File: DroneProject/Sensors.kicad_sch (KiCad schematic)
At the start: 21 parts, among them U61 LSM6DSOTR, U62 TMAG5273C1QDBVR, U63 INA181A1IDBVR, U64 M24C02-WMN6TP

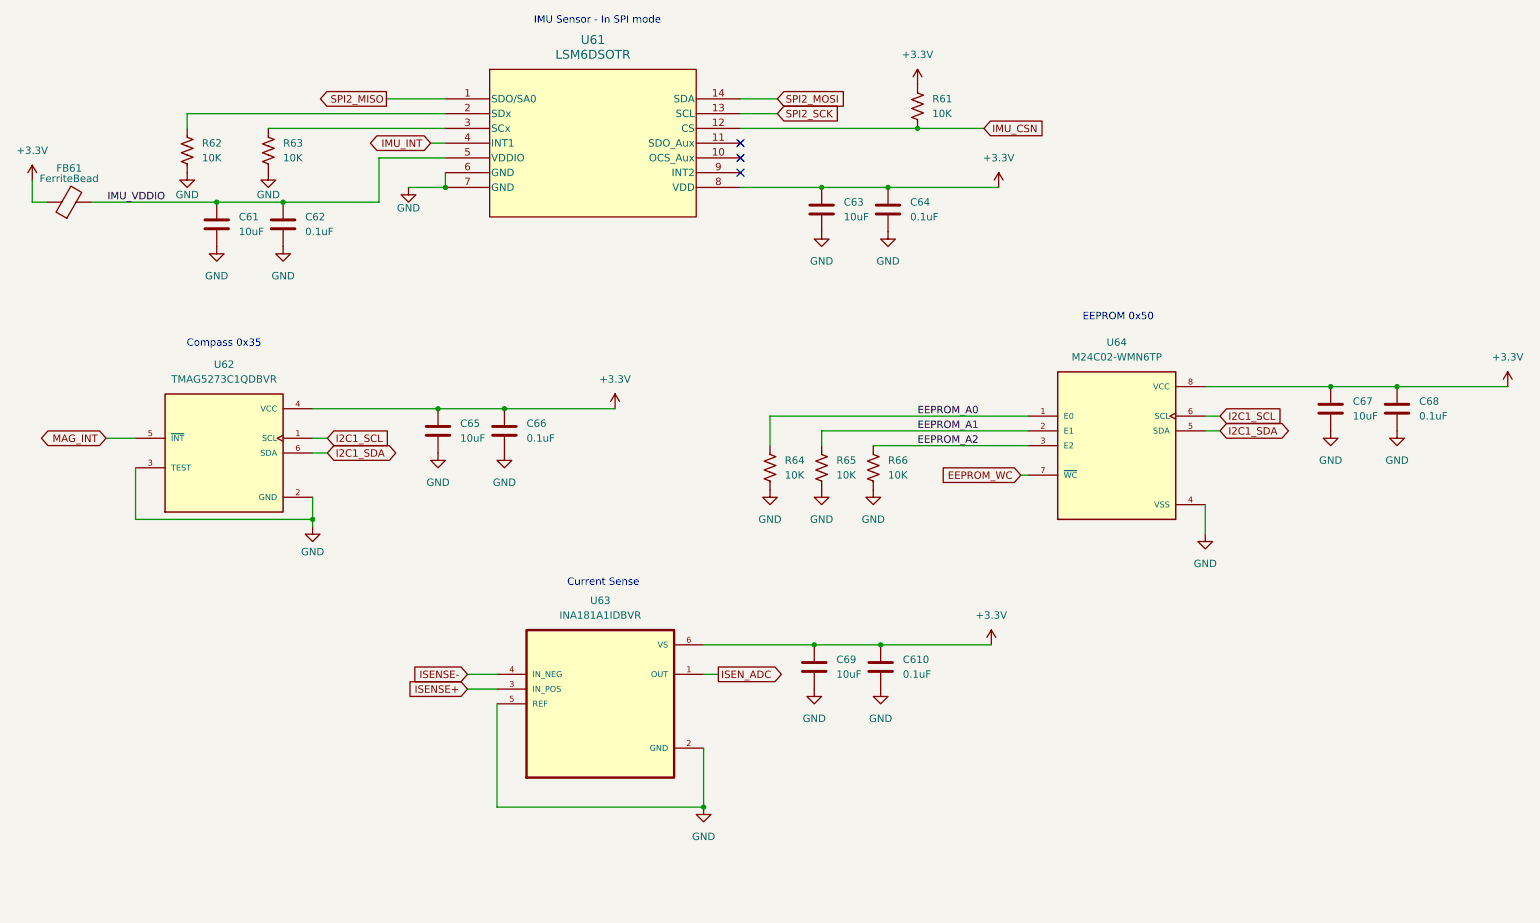
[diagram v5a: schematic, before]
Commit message: Changed motor controller to higher pin count MCU.  Defined all the pins for 3x PWM control over 4 motors.  Renamed a couple of global IO signals to indicate MCU origin (C0 vs C1)
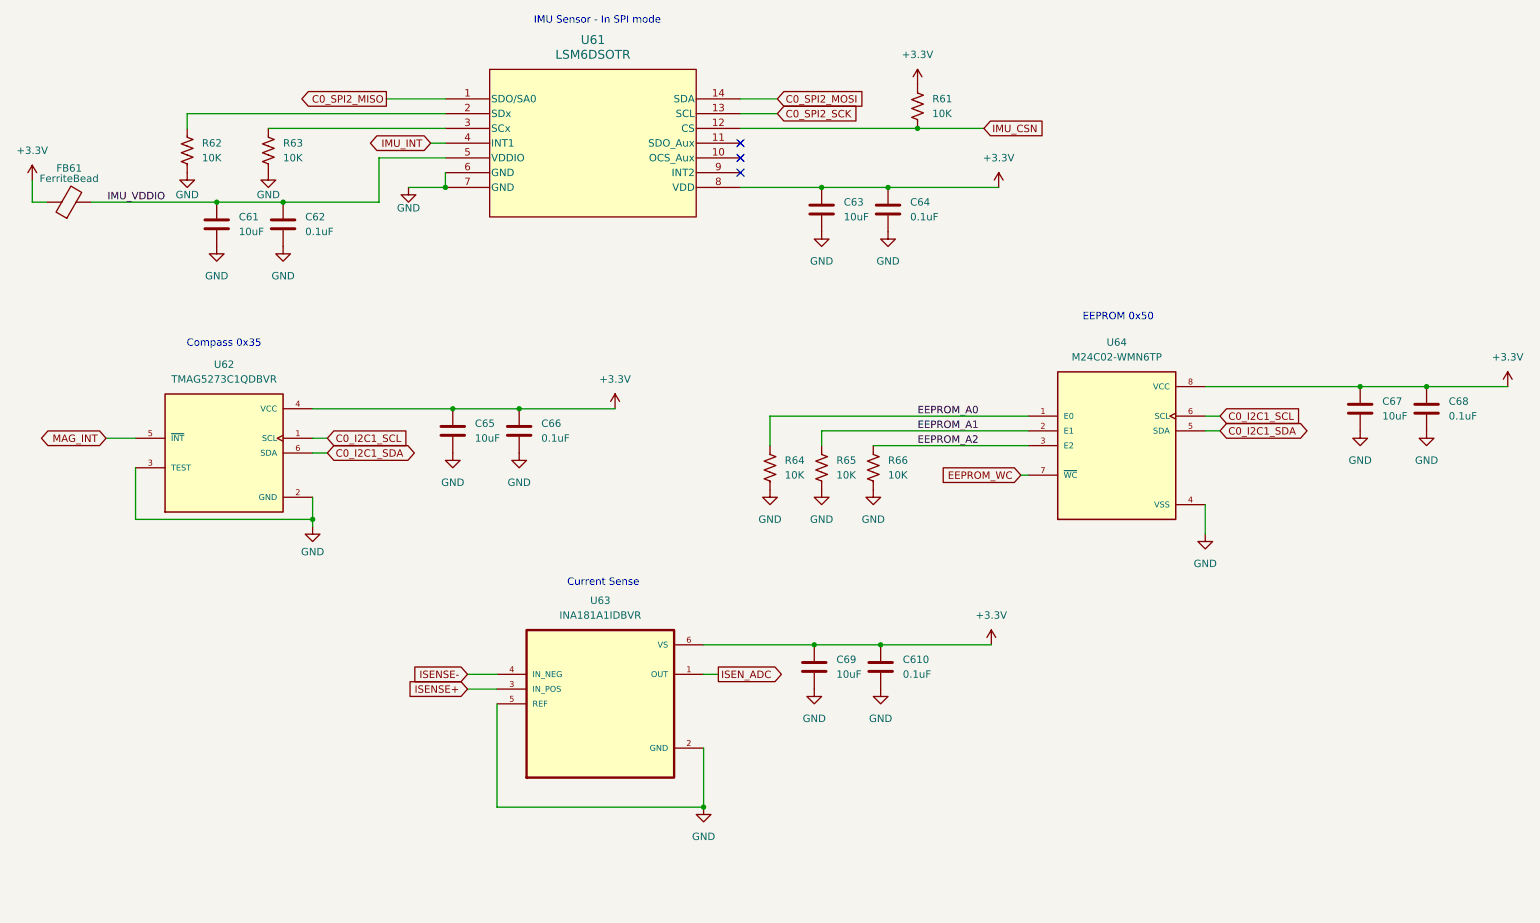
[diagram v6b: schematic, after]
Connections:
- net I2C1_SCL renamed C0_I2C1_SCL
- net I2C1_SDA renamed C0_I2C1_SDA
- net SPI2_MISO renamed C0_SPI2_MISO
- net SPI2_MOSI renamed C0_SPI2_MOSI
- net SPI2_SCK renamed C0_SPI2_SCK
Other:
- moved on the sheet: C65, C66, C67, C68

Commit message: Completed schematic for brushless ESC and added needed components to main board.  The plan is to mount the ESCs on the main board using 2.54mm Vert Conn Headers
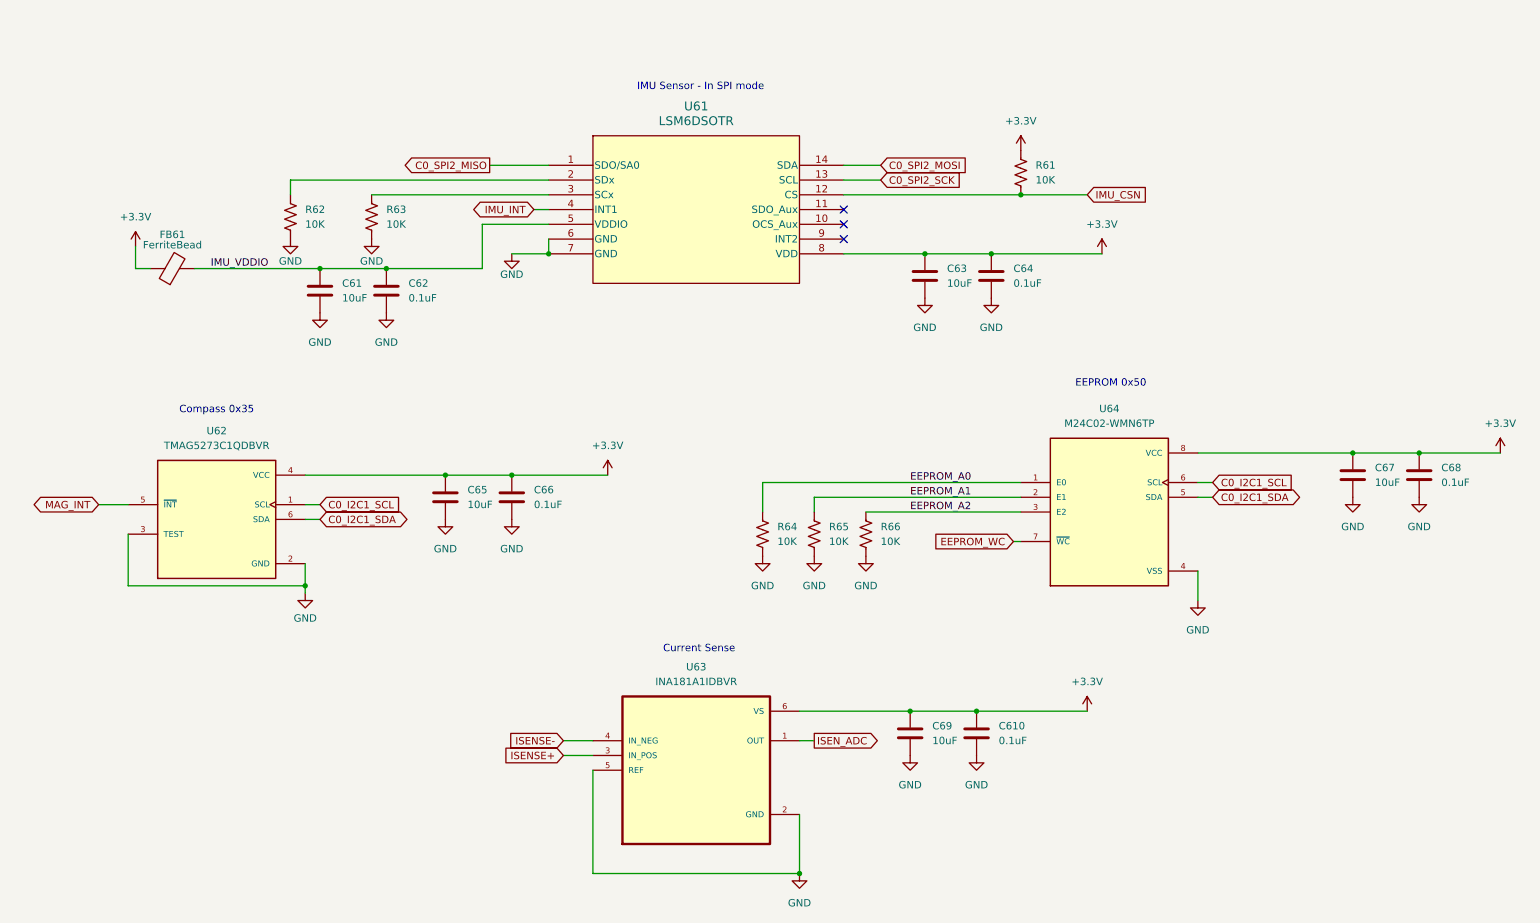
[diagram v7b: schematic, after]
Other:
- moved on the sheet: C61, C610, C62, C63, C64, C65, C66, C67, C68, C69, FB61, R61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

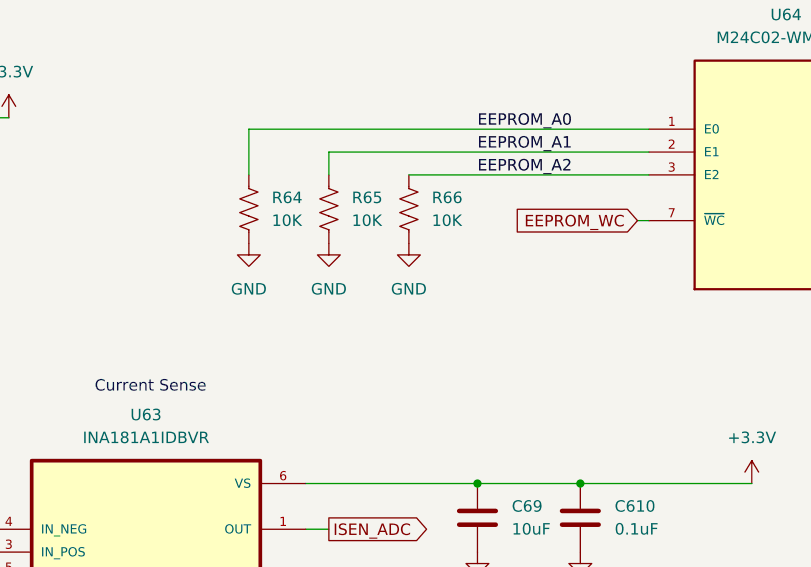
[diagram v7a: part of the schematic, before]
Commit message: Finished brushless driver layout
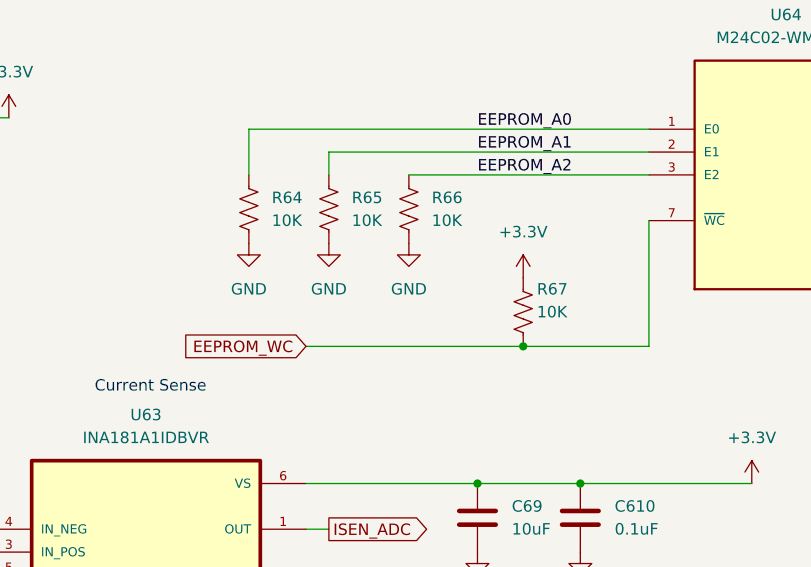
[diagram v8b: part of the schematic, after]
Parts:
- added R67: 10K, Resistor_SMD:R_0402_1005Metric, symbol Device:R_US
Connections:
- net +3.3V: now also R67.2
- net EEPROM_WC: now also R67.1
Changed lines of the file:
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@@
 	)
 	(junction
+		(at 180.34 119.38)
+		(diameter 0)
+		(color 0 0 0 0)
+	)
+	(junction
 		(at 71.12 113.03)
 		(diameter 0)
@@
 	(wire
 		(pts
+			(xy 180.34 119.38) (xy 194.31 119.38)
+		)
+		(stroke
+			(width 0)
+			(type default)
+		)
+	)
+	(wire
+		(pts
 			(xy 106.68 55.88) (xy 113.03 55.88)
 		)
@@
 	(wire
 		(pts
-			(xy 193.04 105.41) (xy 194.31 105.41)
+			(xy 156.21 119.38) (xy 180.34 119.38)
 		)
 		(stroke
@@
 	(wire
 		(pts
+			(xy 194.31 119.38) (xy 194.31 105.41)
+		)
+		(stroke
+			(width 0)
+			(type default)
+		)
+	)
+	(wire
+		(pts
 			(xy 71.12 101.6) (xy 73.66 101.6)
 		)
@@
 	(global_label "EEPROM_WC"
 		(shape input)
-		(at 193.04 105.41 180)
+		(at 156.21 119.38 180)
 		(fields_autoplaced yes)
 		(effects
@@
 		)
 		(property "Intersheetrefs" "${INTERSHEET_REFS}"
-			(at 178.7459 105.41 0)
+			(at 141.9159 119.38 0)
 			(effects
 				(font
@@
 	)
 	(symbol
+		(lib_id "Device:R_US")
+		(at 180.34 115.57 180)
+		(unit 1)
+		(exclude_from_sim no)
+		(in_bom yes)
+		(on_board yes)
+		(dnp no)
+		(property "Reference" "R67"
+			(at 181.864 113.03 0)
+			(effects
+				(font
+					(size 1.27 1.27)
+				)
+				(justify right)
+			)
+		)
+		(property "Value" "10K"
+			(at 181.864 115.57 0)
+			(effects
+				(font
+					(size 1.27 1.27)
+				)
+				(justify right)
+			)
+		)
+		(property "Footprint" "Resistor_SMD:R_0402_1005Metric"
+			(at 179.324 115.316 90)
+			(effects
+				(font
+					(size 1.27 1.27)
+				)
+				(hide yes)
+			)
+		)
+		(property "Datasheet" "~"
+			(at 180.34 115.57 0)
+			(effects
+				(font
+					(size 1.27 1.27)
+				)
+				(hide yes)
+			)
+		)
+		(property "Description" "Resistor, US symbol"
+			(at 180.34 115.57 0)
+			(effects
+				(font
+					(size 1.27 1.27)
+				)
+				(hide yes)
+			)
+		)
+		(pin "1"
+		)
+		(pin "2"
+		)
+		(instances
+			(project "DroneProject"
+				(path "/feb4ca7b-5376-4689-a73b-f56020a5aa30/7cfdeeab-6878-42e6-abbb-2c878b968332"
+					(reference "R67")
+					(unit 1)
+				)
+			)
+		)
+	)
+	(symbol
 		(lib_id "power:GND")
 		(at 71.12 114.3 0)
@@
 					(unit 1)
 				)
+			)
+		)
+	)
+	(symbol
+		(lib_id "power:+3.3V")
+		(at 180.34 111.76 0)
+		(unit 1)
+		(exclude_from_sim no)
+		(in_bom yes)
+		(on_board yes)
+		(dnp no)
+		(fields_autoplaced yes)
+		(property "Reference" "#PWR0118"
+			(at 180.34 115.57 0)
+			(effects
+				(font
+					(size 1.27 1.27)
+				)
+				(hide yes)
+			)
+		)
+		(property "Value" "+3.3V"
+			(at 180.34 106.68 0)
+			(effects
+				(font
+					(size 1.27 1.27)
+				)
+			)
+		)
+		(property "Footprint" ""
+			(at 180.34 111.76 0)
+			(effects
+				(font
+					(size 1.27 1.27)
+				)
+				(hide yes)
+			)
+		)
+		(property "Datasheet" ""
+			(at 180.34 111.76 0)
+			(effects
+				(font
+					(size 1.27 1.27)
+				)
+				(hide yes)
+			)
+		)
+		(property "Description" "Power symbol creates a global label with name \"+3.3V\""
+			(at 180.34 111.76 0)
+			(effects
+				(font
+					(size 1.27 1.27)
+				)
+				(hide yes)
+			)
+		)
+		(pin "1"
+		)
+		(instances
+			(project "DroneProject"
+				(path "/feb4ca7b-5376-4689-a73b-f56020a5aa30/7cfdeeab-6878-42e6-abbb-2c878b968332"
+					(reference "#PWR0118")
+					(unit 1)
+				)
